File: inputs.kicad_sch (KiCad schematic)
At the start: 46 parts, among them J1 Conn_01x15, J2 2601-3106, J3 2601-3109, J4 HTSW-217-15-T-S, U1 PC817, U10 PC817, U11 PC817, U12 PC817, U13 PC817, U14 PC817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

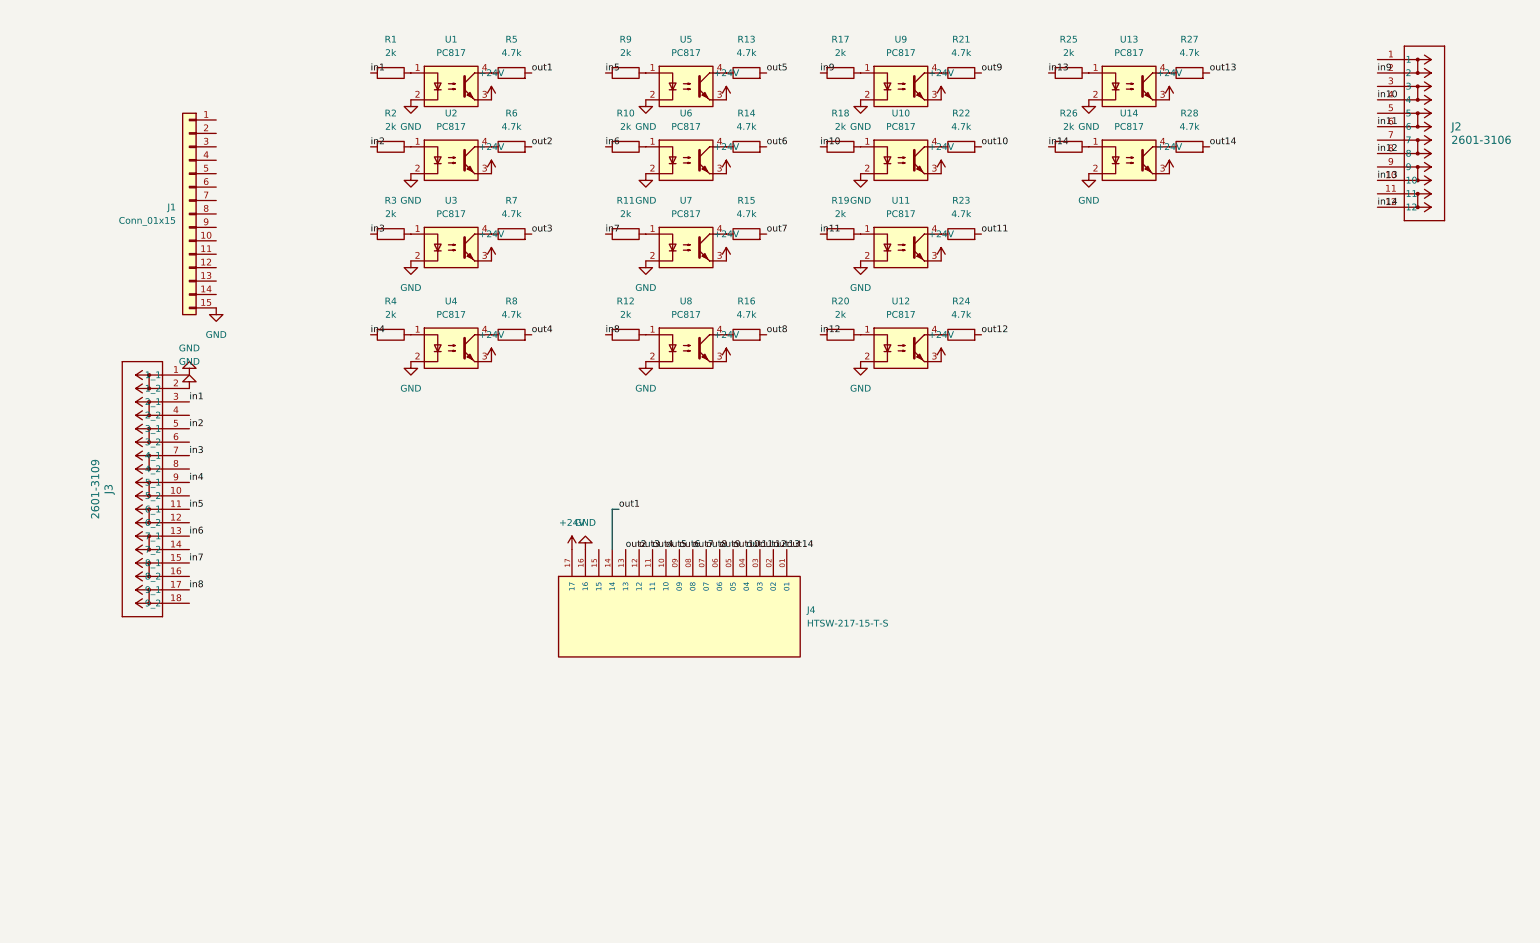
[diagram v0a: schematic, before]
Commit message: Move to 2 8Pin Wagos
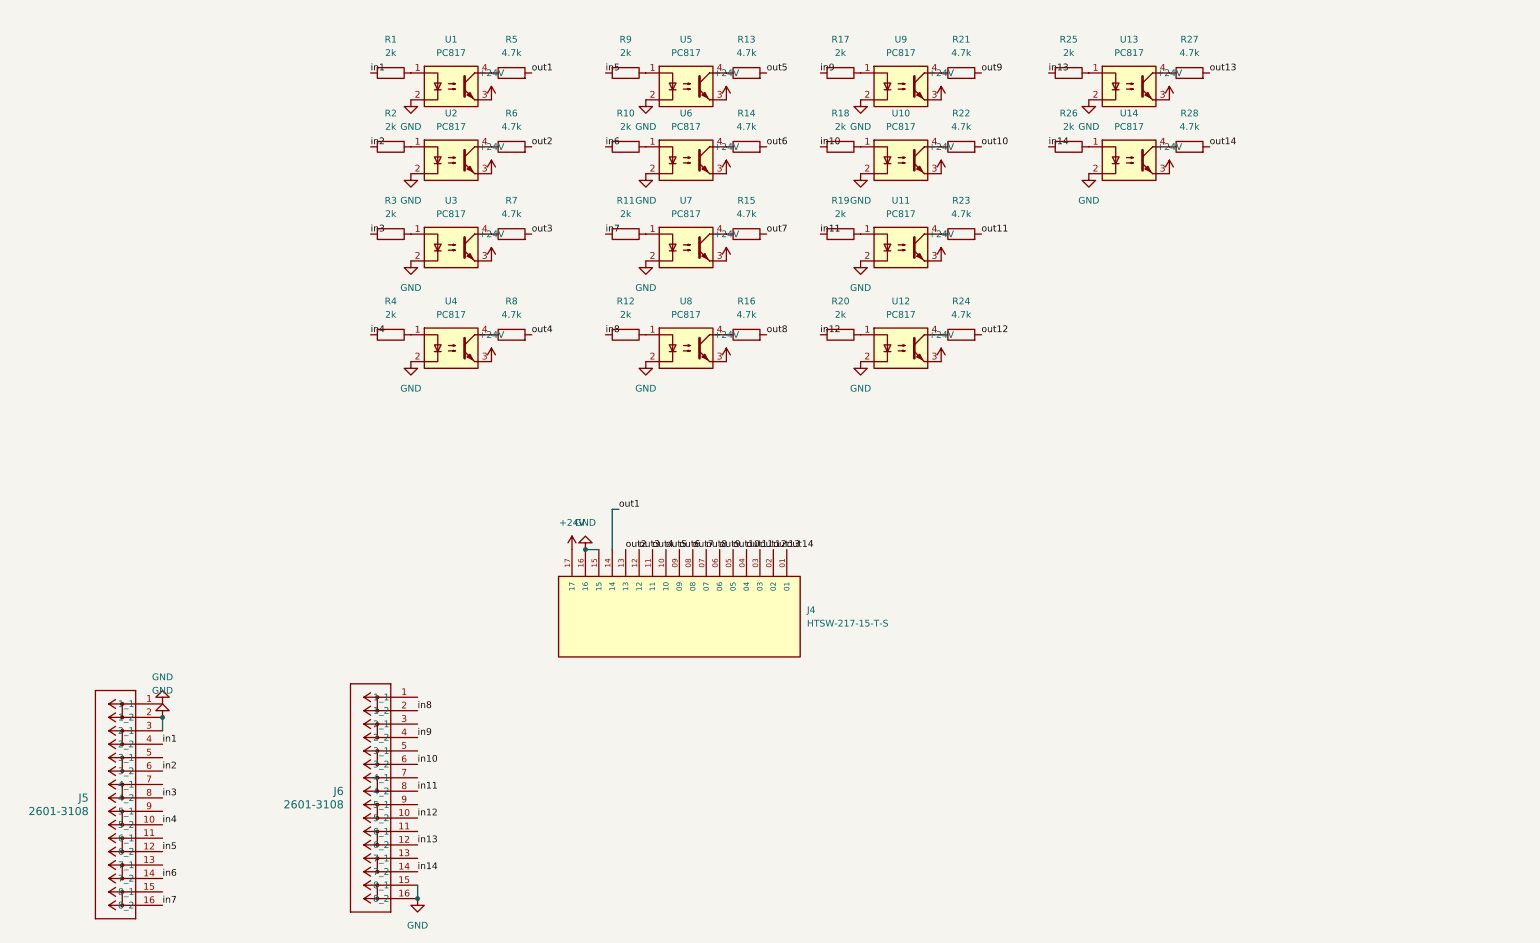
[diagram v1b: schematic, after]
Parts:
- removed J1: Conn_01x15, Connector_PinHeader_2.54mm:PinHeader_1x15_P2.54mm_Vertical, symbol Connector_Generic:Conn_01x15
- removed J2: 2601-3106, CONN_2601-3106_WAG, symbol 3106:2601-3106
- removed J3: 2601-3109, CONN9_2601-3109_WAG, symbol 3109:2601-3109
- added J5, J6: 2601-3108, 3108:CONN8_2601-3108_WAG, symbol 3108:2601-3108
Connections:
- net GND: now also J4.15, J5.1 (1_1), J5.2 (1_2), J5.3 (2_1), J6.15 (8_1), J6.16 (8_2)
- net in1: now also J5.4 (2_2)
- net in10: now also J6.6 (3_2)
- net in11: now also J6.8 (4_2)
- net in12: now also J6.10 (5_2)
- net in13: now also J6.12 (6_2)
- net in14: now also J6.14 (7_2)
- net in2: now also J5.6 (3_2)
- net in3: now also J5.8 (4_2)
- net in4: now also J5.10 (5_2)
- net in5: now also J5.12 (6_2)
- net in6: now also J5.14 (7_2)
- net in7: now also J5.16 (8_2)
- net in8: now also J6.2 (1_2)
- net in9: now also J6.4 (2_2)

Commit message: Add Common GND Jumpers, split 5v/24v, Add LEDS
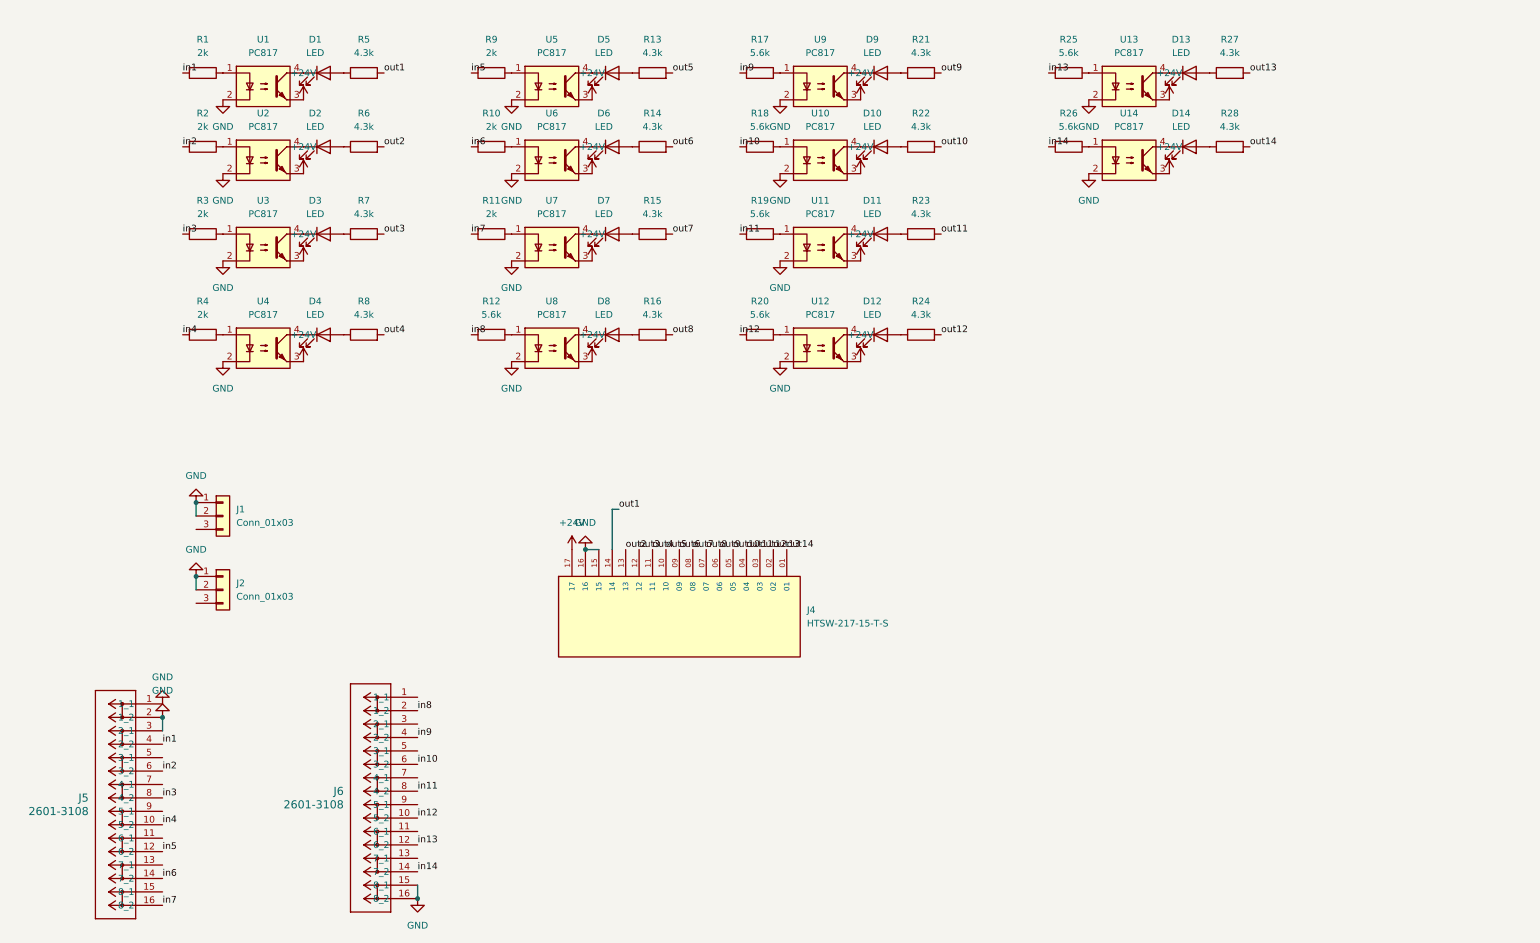
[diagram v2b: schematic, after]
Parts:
- added D1, D10, D11, D12, D13, D14, D2, D3, D4, D5, D6, D7, D8, D9: LED, LED_SMD:LED_0805_2012Metric, symbol Device:LED
- added J1, J2: Conn_01x03, Connector_PinHeader_2.54mm:PinHeader_1x03_P2.54mm_Vertical, symbol Connector_Generic:Conn_01x03
- R12, R17, R18, R19, R20, R25, R26: value 2k -> 5.6k
- R13, R14, R15, R16, R21, R22, R23, R24, R27, R28, R5, R6, R7, R8: value 4.7k -> 4.3k
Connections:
- net GND: now also J1.1 (Pin_1), J1.2 (Pin_2), J2.1 (Pin_1), J2.2 (Pin_2)
- net at U12.4: now also D12.1 (K); no longer R24.1
- net at R5.1: now also D1.2 (A); no longer U1.4
- net at R6.1: now also D2.2 (A); no longer U2.4
- net at R7.1: now also D3.2 (A); no longer U3.4
- net at R22.1: now also D10.2 (A); no longer U10.4
- net at R23.1: now also D11.2 (A); no longer U11.4
- net at R15.1: now also D7.2 (A); no longer U7.4
- net at R21.1: now also D9.2 (A); no longer U9.4
- net at U4.4: now also D4.1 (K); no longer R8.1
- net at R28.1: now also D14.2 (A); no longer U14.4
- net at U13.4: now also D13.1 (K); no longer R27.1
- net at U6.4: now also D6.1 (K); no longer R14.1
- net at U8.4: now also D8.1 (K); no longer R16.1
- net at U5.4: now also D5.1 (K); no longer R13.1
- new net: D8.2 (A), R16.1
- new net: D3.1 (K), U3.4
- new net: D11.1 (K), U11.4
- new net: D12.2 (A), R24.1
- new net: D2.1 (K), U2.4
- new net: D6.2 (A), R14.1
- new net: D9.1 (K), U9.4
- new net: D10.1 (K), U10.4
- new net: D7.1 (K), U7.4
- new net: D13.2 (A), R27.1
- new net: D1.1 (K), U1.4
- new net: D4.2 (A), R8.1
- new net: D5.2 (A), R13.1
- new net: D14.1 (K), U14.4
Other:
- moved on the sheet: R1, R10, R11, R12, R13, R14, R15, R16, R17, R18, R19, R2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

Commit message: update Silkscreen, update values
First board ordered
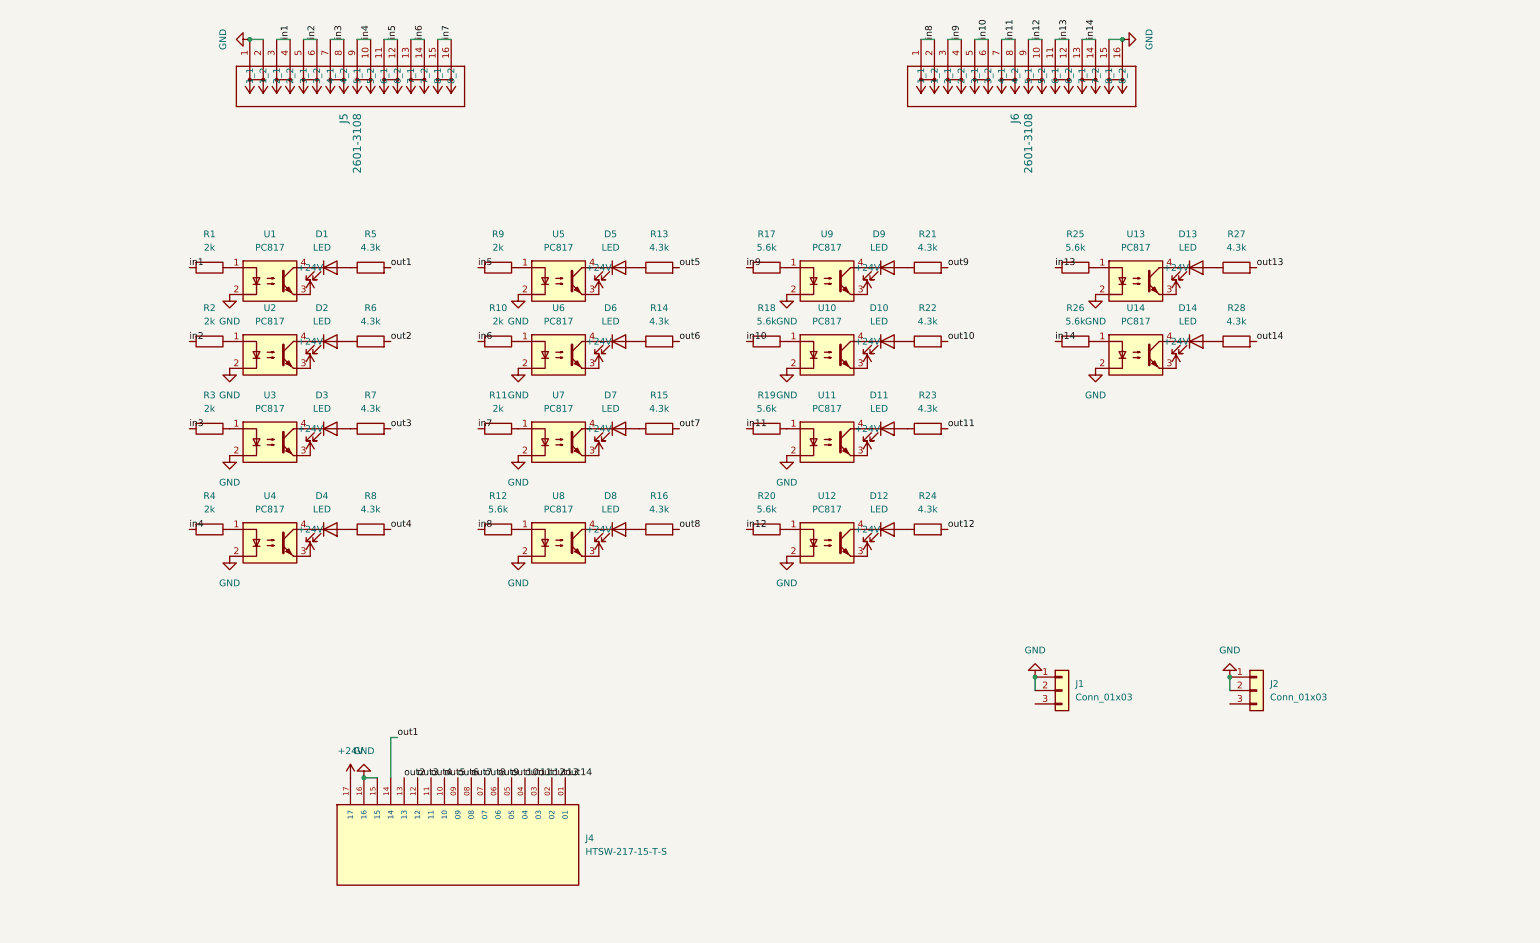
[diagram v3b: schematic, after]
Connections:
- net GND: no longer J5.3 (2_1)
- net in1: now also J5.3 (2_1)
- net in10: now also J6.5 (3_1)
- net in11: now also J6.7 (4_1)
- net in12: now also J6.9 (5_1)
- net in13: now also J6.11 (6_1)
- net in14: now also J6.13 (7_1)
- net in2: now also J5.5 (3_1)
- net in3: now also J5.7 (4_1)
- net in4: now also J5.9 (5_1)
- net in5: now also J5.11 (6_1)
- net in6: now also J5.13 (7_1)
- net in7: now also J5.15 (8_1)
- net in8: now also J6.1 (1_1)
- net in9: now also J6.3 (2_1)
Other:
- moved on the sheet: D1, D10, D11, D12, D13, D14, D2, D3, D4, D5, D6, D7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
